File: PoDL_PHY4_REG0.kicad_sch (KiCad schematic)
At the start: 29 parts, among them Q25 DMG3414U, Q26 MMBTA06, Q27 MMBT3904, Q28 DMG3414U, Q29 DMG3414U, Q30 MMBT3904, Q31 SiS412DN, U14 LTC4296-1

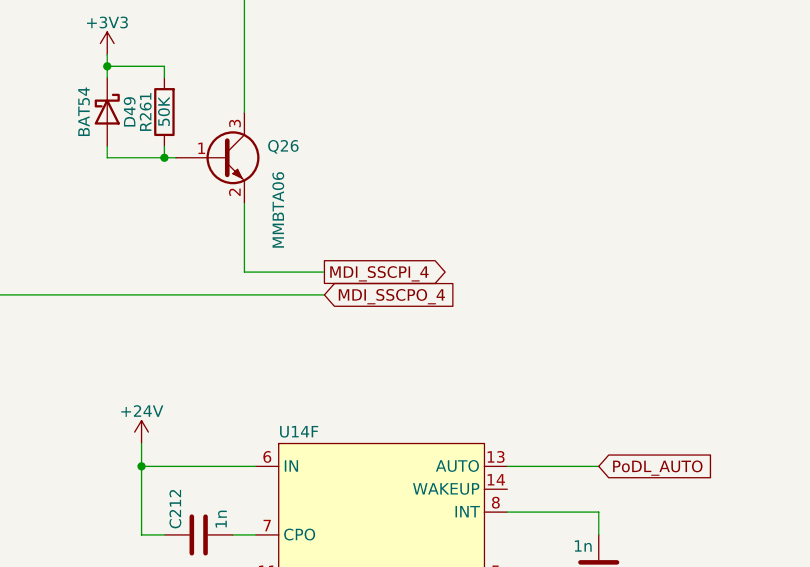
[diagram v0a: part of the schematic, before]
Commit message: Correcting SCCP spelling
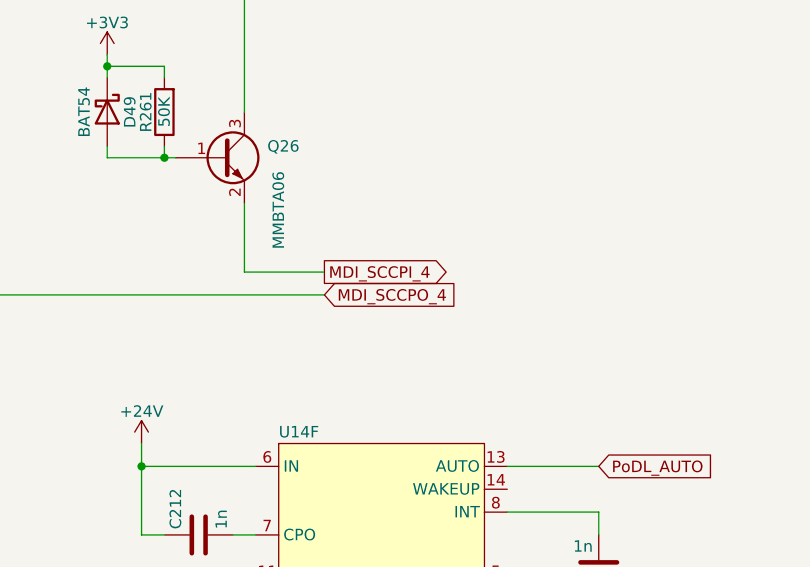
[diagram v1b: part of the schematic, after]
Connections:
- net MDI_SSCPI_4 renamed MDI_SCCPI_4
- net MDI_SSCPO_4 renamed MDI_SCCPO_4
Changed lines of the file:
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@@
     (effects (font (size 1.27 1.27) bold) (justify left bottom))
   )
-  (global_label "MDI_SSCPI_4" (shape output) (at 198.12 58.42 0) (fields_autoplaced)
+  (global_label "MDI_SCCPI_4" (shape output) (at 198.12 58.42 0) (fields_autoplaced)
     (effects (font (size 1.27 1.27)) (justify left))
     (property "Intersheet References" "${INTERSHEET_REFS}" (id 0) (at 212.5679 58.3406 0)
@@
     )
   )
-  (global_label "MDI_SSCPO_4" (shape input) (at 198.12 60.96 0) (fields_autoplaced)
+  (global_label "MDI_SCCPO_4" (shape input) (at 198.12 60.96 0) (fields_autoplaced)
     (effects (font (size 1.27 1.27)) (justify left))
     (property "Intersheet References" "${INTERSHEET_REFS}" (id 0) (at 213.2936 60.8806 0)
